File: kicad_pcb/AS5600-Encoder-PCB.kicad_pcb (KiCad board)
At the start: 2 copper layers, 26 x 17.1 mm, 12 parts, among them IC1 AS5600-ASOM, J1 Conn_01x04_Male, J2 Conn_01x04_Male

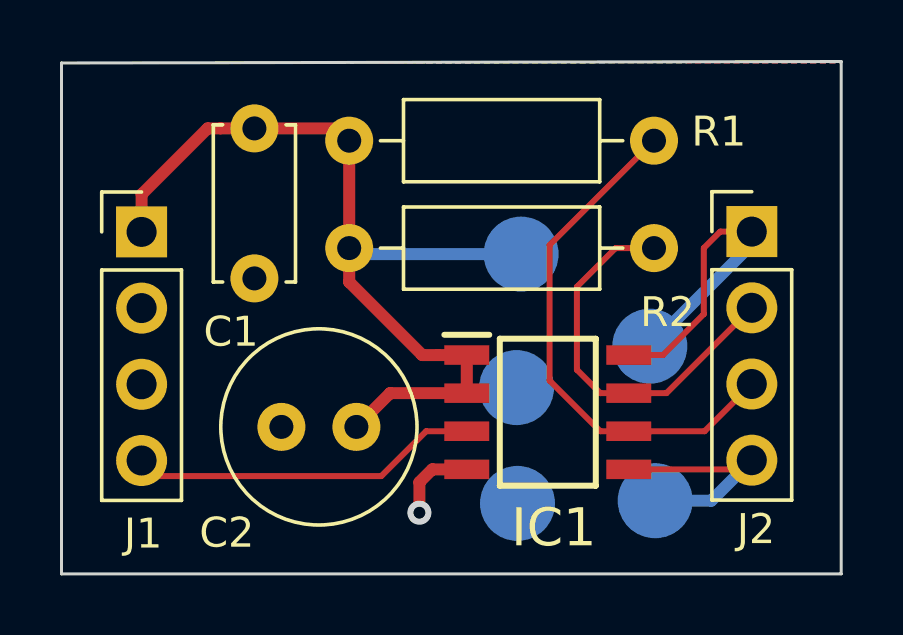
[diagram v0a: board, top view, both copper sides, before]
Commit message: Added SMD PCB for AS5600 Controller Board
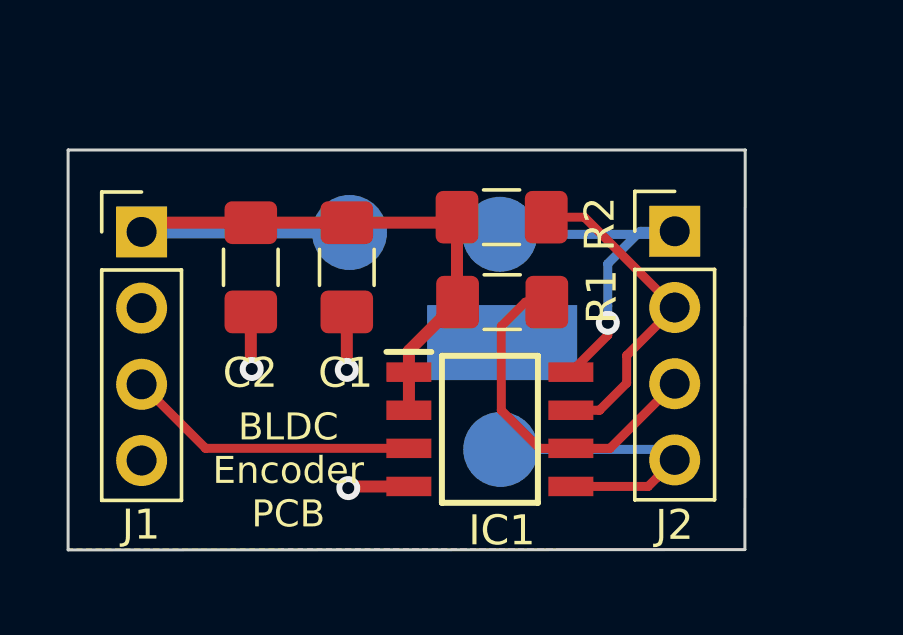
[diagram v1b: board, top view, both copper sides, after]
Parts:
- removed the GND at (205.4, 160.4)
- C1: footprint Capacitor_THT:C_Disc_D5.0mm_W2.5mm_P5.00mm -> Capacitor_SMD:C_1206_3216Metric_Pad1.42x1.75mm_HandSolder
- C2: footprint Capacitor_THT:C_Radial_D6.3mm_H11.0mm_P2.50mm -> Capacitor_SMD:C_1206_3216Metric_Pad1.42x1.75mm_HandSolder
- R1, R2: footprint Resistor_THT:R_Axial_DIN0207_L6.3mm_D2.5mm_P10.16mm_Horizontal -> Resistor_SMD:R_1206_3216Metric_Pad1.42x1.75mm_HandSolder
- moved R1 7.41 mm to (204.9, 153.7)
- moved C2 6.38 mm to (196.5, 152.5), turned to 270 degrees
- moved DIR 6.24 mm to (204.8, 151.4)
- moved 3V3 5.77 mm to (199.8, 151.4)
- moved PGO 5.43 mm to (204.9, 158.6)
- moved R2 5.18 mm to (204.9, 150.9)
- moved C1 3.10 mm to (199.7, 152.5)
- moved J2 2.57 mm to (210.7, 151.3)
- moved IC1 2.01 mm to (204.5, 157.9)
- moved GND 1.57 mm to (204.9, 155.0)
- renumbered VCC(3V3) to 3V3
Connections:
- J1 pad 3: GND -> /OUT
- J1 pad 4: /OUT -> GND
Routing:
- net /SDA: track 17.5 -> 11.8 mm
- net +3V3: track 30.1 -> 24.9 mm
- net GND: track 2.77 -> 6.40 mm, vias 1 -> 3
- net /PGO: track 8.01 -> 10.6 mm
- net /OUT: track 11.7 -> 9.79 mm
- net /SCL: track 13.2 -> 11.5 mm
- net /DIR: vias 0 -> 1
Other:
- board size 26 x 17.1 mm -> 22.6 x 13.3 mm
- board text added: "BLDC Encoder PCB"
- board text added: "SRA VJTI"

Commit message: Added holes, gerbers - SMD PCB
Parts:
- added REF**: OSHW-Logo2_7.3x6mm_SilkScreen, Symbol:OSHW-Logo2_7.3x6mm_SilkScreen, F.Cu at (197.9, 160.2)
- added REF**: MountingHole_2.1mm, MountingHole:MountingHole_2.1mm, F.Cu at (211.4, 148.3)
- added REF**: MountingHole_2.1mm, MountingHole:MountingHole_2.1mm, F.Cu at (192.3, 148.4)
- added REF**: MountingHole_2.1mm, MountingHole:MountingHole_2.1mm, F.Cu at (211.4, 162.1)
- added |: MountingHole_2.1mm, MountingHole:MountingHole_2.1mm, F.Cu at (192.3, 162.1)
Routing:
- net GND: track 6.40 -> 7.98 mm
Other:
- board size 22.6 x 13.3 mm -> 22.6 x 16.8 mm
- board text added: "---> CLK"
- board text added: "--> CCLK"
- board text added: "1"
- board text added: "SRA-VJTI"
- board text added: "TitanLegs"
- board text removed: "SRA VJTI"
- board text removed: "______> CLK"
- board text removed: "_______> CCLK"

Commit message: Made suggested changes
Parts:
- removed the REF** at (197.9, 160.2)
- removed the REF** at (211.4, 148.3)
- removed the REF** at (192.3, 148.4)
- removed the REF** at (211.4, 162.1)
- removed |: MountingHole_2.1mm, MountingHole:MountingHole_2.1mm
- added ?: , , F.Cu at (201.6, 145.2)
- added ?: , , F.Cu at (200.4, 149.2)
- added ?: , , F.Cu at (195.2, 150.5)
- added ?: , , F.Cu at (194.0, 149.2)
- added REF**: MountingHole_2.1mm, MountingHole:MountingHole_2.1mm, F.Cu at (211.5, 148.4)
- added REF**: MountingHole_2.1mm, MountingHole:MountingHole_2.1mm, F.Cu at (211.5, 162.0)
- added REF**: MountingHole_2.1mm, MountingHole:MountingHole_2.1mm, F.Cu at (192.1, 162.0)
- added REF**: MountingHole_2.1mm, MountingHole:MountingHole_2.1mm, F.Cu at (192.2, 148.4)
- R1, R2: footprint Resistor_SMD:R_1206_3216Metric_Pad1.42x1.75mm_HandSolder -> Resistor_SMD:R_0603_1608Metric_Pad1.05x0.95mm_HandSolder
- moved IC1 2.74 mm to (201.8, 157.9)
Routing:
- net /SCL: track 11.5 -> 15.5 mm
- net +3V3: track 24.9 -> 28.0 mm
- net /DIR: track 12.7 -> 15.8 mm
- net /OUT: track 9.79 -> 7.05 mm
- net /PGO: track 10.6 -> 13.4 mm
- net /SDA: track 11.8 -> 13.1 mm
- net GND: track 7.98 -> 7.44 mm

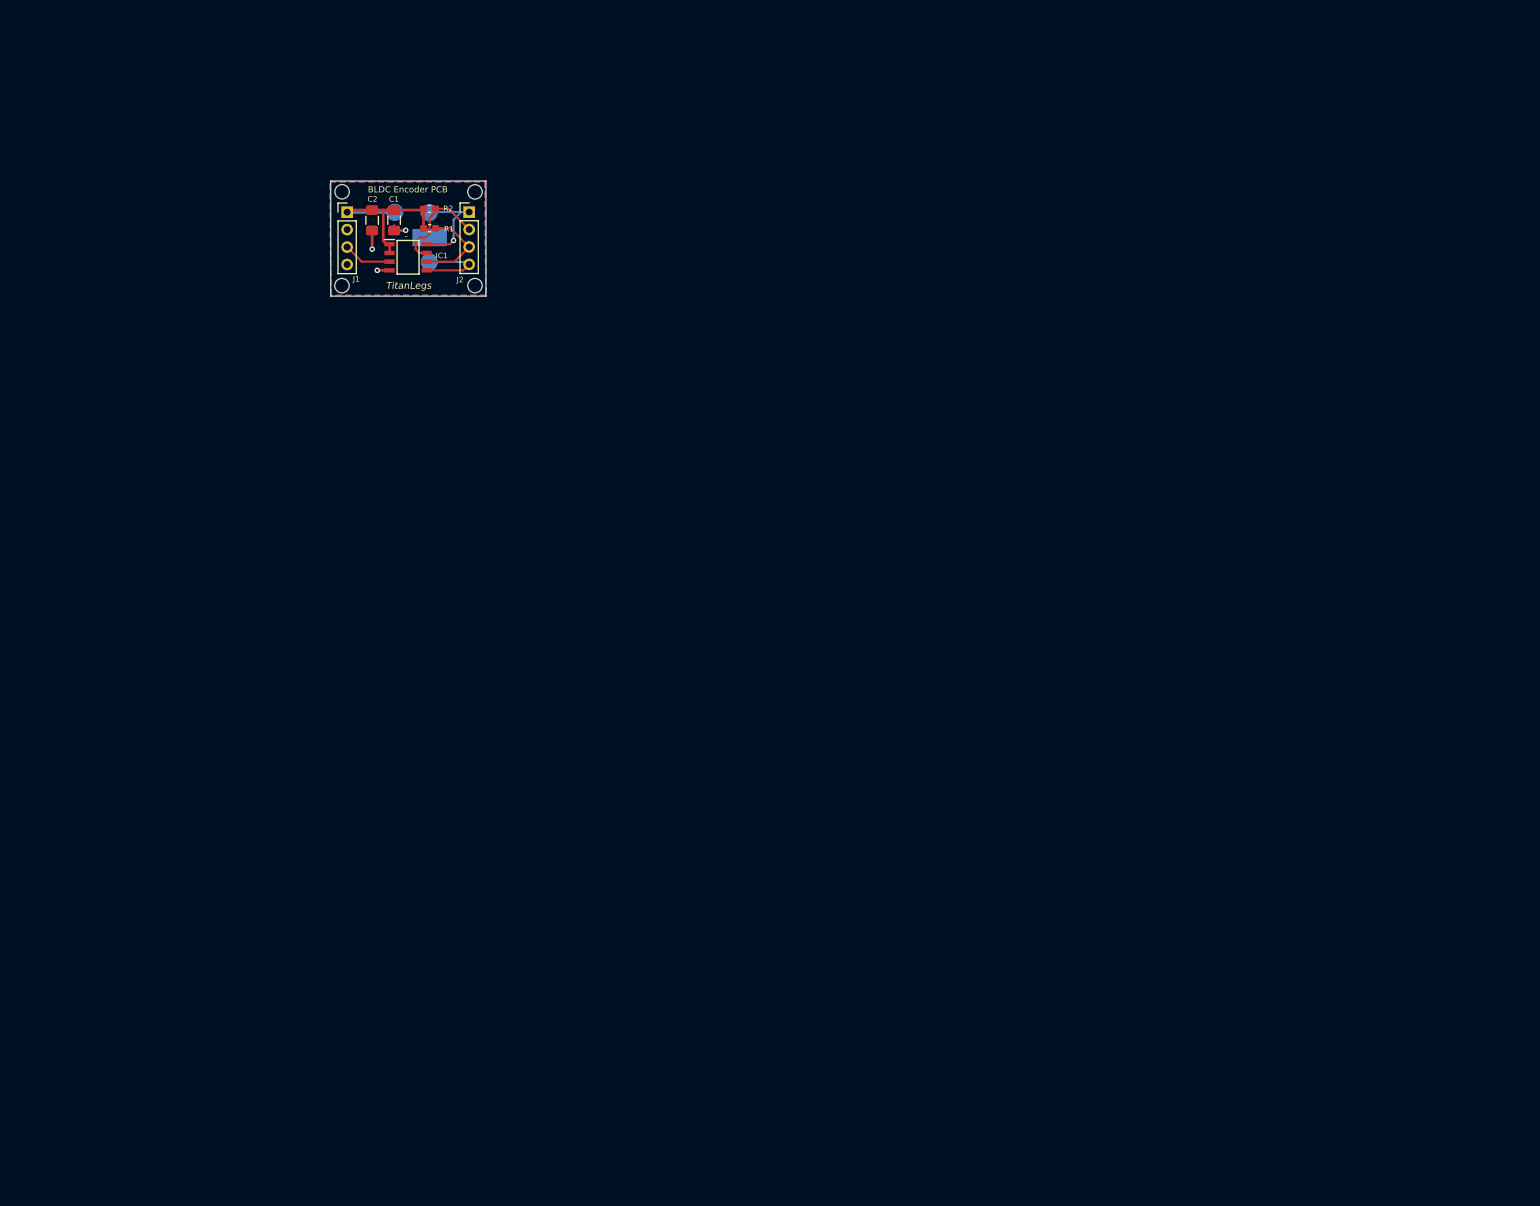
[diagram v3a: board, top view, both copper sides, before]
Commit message: Modified and optimized design for 1 layer
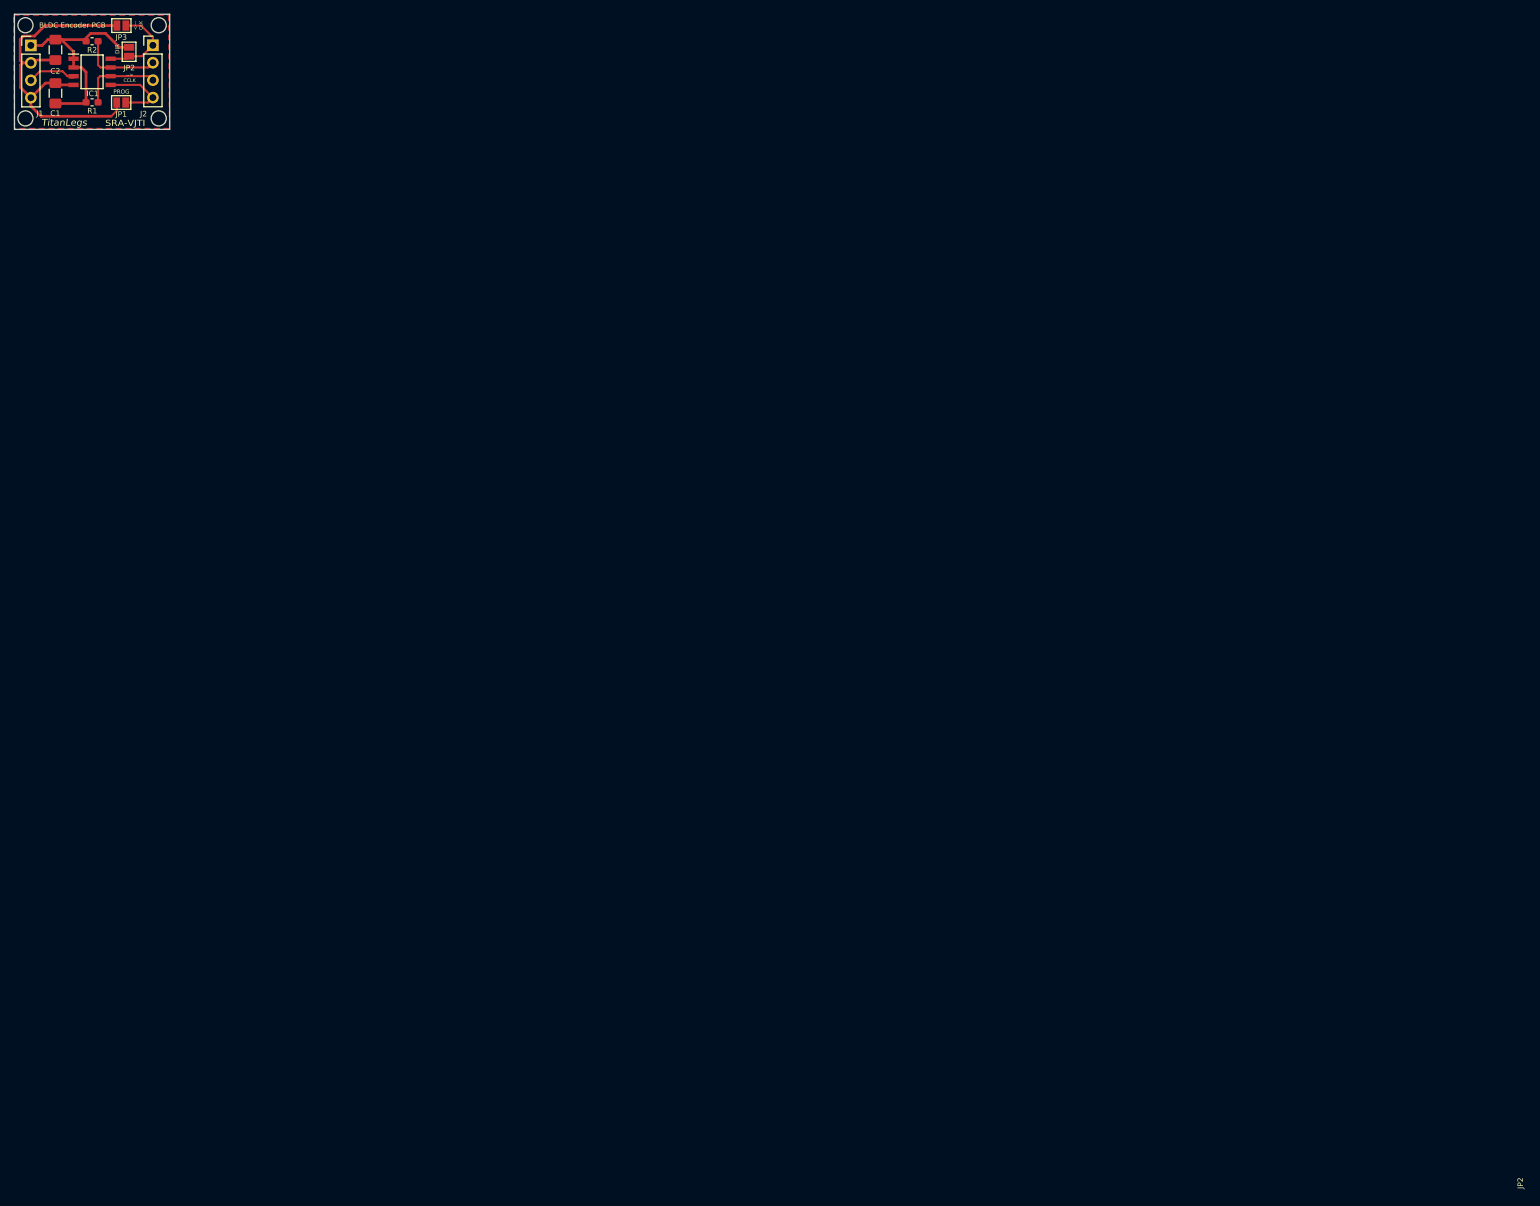
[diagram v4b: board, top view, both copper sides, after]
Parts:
- removed 3V3, DIR, GND, PGO: TestPoint, TestPoint:TestPoint_Pad_D2.5mm
- removed the ? at (201.6, 145.2)
- removed the ? at (200.4, 149.2)
- removed the ? at (195.2, 150.5)
- removed the ? at (194.0, 149.2)
- removed REF** (x4): MountingHole_2.1mm, MountingHole:MountingHole_2.1mm
- added ?: , , F.Cu at (161.2, 130.0)
- added H1: MountingHole, MountingHole:MountingHole_2.2mm_M2, F.Cu at (146.1, 124.1)
- added H2: MountingHole, MountingHole:MountingHole_2.2mm_M2, F.Cu at (165.5, 124.1)
- added H3: MountingHole, MountingHole:MountingHole_2.2mm_M2, F.Cu at (146.1, 137.7)
- added H4: MountingHole, MountingHole:MountingHole_2.2mm_M2, F.Cu at (165.5, 137.7)
- added JP1: SolderJumper_2_Open, Jumper:SolderJumper-2_P1.3mm_Open_Pad1.0x1.5mm, F.Cu at (160.0, 135.4)
- added JP2: SolderJumper_2_Open, Jumper:SolderJumper-2_P1.3mm_Open_Pad1.0x1.5mm, F.Cu at (161.1, 128.0)
- added JP3: SolderJumper_2_Open, Jumper:SolderJumper-2_P1.3mm_Open_Pad1.0x1.5mm, F.Cu at (160.0, 124.2)
- moved R2 54.9 mm to (155.8, 126.5)
- moved IC1 53.3 mm to (155.8, 130.9)
- moved C1 52.7 mm to (150.4, 134.0), turned to 270 degrees
- moved R1 52.5 mm to (155.8, 135.4)
- moved C2 52.4 mm to (150.4, 127.7)
- moved J1 52.1 mm to (146.8, 127.1)
- moved J2 52.1 mm to (164.6, 127.0)
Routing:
- net GND: track 7.44 -> 52.3 mm, vias 3 -> 0
- net +3V3: track 28.0 -> 33.1 mm
- net /SCL: track 15.5 -> 12.4 mm
- net /DIR: track 15.8 -> 12.8 mm, vias 1 -> 0
- net /PGO: track 13.4 -> 11.7 mm
- net /SDA: track 13.1 -> 11.9 mm
- removed copper zone on B.Cu, net GND
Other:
- board text added: "<--- CLK"
- board text added: "DIR"
- board text added: "PROG"
- board text removed: "---> CLK"

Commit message: Added PCB layout dimensions
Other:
- net class Default removed
